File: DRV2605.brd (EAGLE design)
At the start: 49.9 x 25 mm, 60 parts, among them J1 BM06B-SRSS-TB, J2 BM06B-SRSS-TB, J3 BM06B-SRSS-TB, J4 BM06B-SRSS-TB, J5 BM06B-SRSS-TB, U1 DRV2605L, U2 DRV2605L, U3 DRV2605L, U4 DRV2605L, U5 DRV2605L, U6 DRV2605L, U7 DRV2605L, U8 TCA9548APWR, U9 TCA9548APWR

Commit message: NRF done STM in progress
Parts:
- added C17, C18, C46, C47, C55, C56: 12pF, Nordic_nRF:RESC0402_N
- added C19, C20: 22pF, Nordic_nRF:RESC0402_N
- added C21: 0.1uf, rcl:C0402
- added C22: 10uf, rcl:C0402
- added C23, C24: 2.2uf, rcl:C0402
- added C48: 2.2nF, Nordic_nRF:RESC0402_N
- added C49, C52: 100nF, Nordic_nRF:RESC0402_N
- added C50: 47nF, Nordic_nRF:RESC0402_N
- added C51: 1.0nF, Nordic_nRF:RESC0402_N
- added C53: 4.7µF, Nordic_nRF:RESC0603_N
- added C54: 1.0µF, Nordic_nRF:RESC0603_N
- added C57: 2.2pF, Nordic_nRF:RESC0402_N
- added C58: 1.0pF, Nordic_nRF:RESC0402_N
- added C59: 1.5pF, Nordic_nRF:RESC0402_N
- added L11: 3.3nH, Nordic_nRF:RESC0402_N
- added L12: 10µH, Nordic_nRF:RESC0603_N
- added L13: 15nH, Nordic_nRF:RESC0402_N
- added L14: 4.7nH, Nordic_nRF:RESC0402_N
- added L15: 10nH, Nordic_nRF:RESC0402_N
- added R21, R22, R25: 10k, resistor:R0402
- added R23: 1M, resistor:R0402
- added U$9: STM32F405RGT6, SparkFun-IC-Microcontroller:TQFP64
- added U11: NRF51X22_QFQF, Nordic_nRF:QFN40P600X600X90-48_N
- added X1, X5: 32.768kHz, Nordic_nRF:XTAL_3215_N
- added X2: 8MHz, Nordic_nRF:XTAL_3215_N
- added X4: 16MHz, Nordic_nRF:BT-XTAL_2016_N
- moved C13 28.4 mm to (13.2, 13.7), turned to 270 degrees
- moved I2C14 26.0 mm to (14.8, 16.6), turned to 90 degrees
- moved U7 25.7 mm to (15.5, 15.6), turned to 270 degrees
- moved C16 25.6 mm to (37.9, 26.7)
- moved R18 25.1 mm to (38.0, 24.8)
- moved R19 25.1 mm to (38.0, 23.5)
- moved R20 25.1 mm to (38.0, 22.2)
- moved U9 25.1 mm to (43.2, 23.6)
- moved R14 24.2 mm to (16.2, 16.6), turned to 270 degrees
- moved C14 23.6 mm to (17.7, 16.7), turned to 270 degrees
- moved R13 22.4 mm to (17.7, 16.7), turned to 270 degrees
- moved C11 21.3 mm to (19.4, 13.6), turned to 270 degrees
- moved I2C12 18.7 mm to (20.8, 16.6), turned to 90 degrees
- moved U6 18.6 mm to (21.6, 15.5), turned to 270 degrees
- moved R12 17.0 mm to (22.3, 16.5), turned to 270 degrees
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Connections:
- removed net 1SCL: U8.7
- removed net 1SDA: U8.6
- removed net 2SCL: U8.9
- removed net 2SDA: U8.8
- removed net N$22: U8.21
- new net AVDD: C51.1, C54.1, L13.1, U11.35, U11.36
- new net BLE_RX: U$9.42, U11.11
- new net BLE_TX: U$9.43, U11.10
- new net N$2: R25.2, U$9.28
- new net N$3: R22.1, U$9.60
- new net N$33: C46.1, U11.38, X4.3
- new net N$34: L12.1, L13.2
- new net N$35: L12.2, U11.2
- new net N$36: C50.1, U11.29
- new net N$37: C49.1, U11.39
- new net N$38: L14.1, L15.2, U11.31
- new net N$39: C48.1, L15.1, U11.30
- new net N$40: C57.1, L14.2, U11.32
- new net N$41: C57.2, C58.1, L11.1
- new net N$5: C23.1, U$9.31
- new net N$6: C24.1, U$9.47
- new net P0.00: U11.4
- new net P0.01: U11.5
- new net P0.02: U11.6
- new net P0.03: U11.7
- new net P0.04: U11.8
- new net P0.05: U11.9
- new net P0.08: U11.14
- new net P0.09: U11.15
- new net P0.10: U11.16
- new net P0.11: U11.17
- new net P0.12: U11.18
- new net P0.13: U11.19
- new net P0.14: U11.20
- new net P0.17: U11.25
- new net P0.19: U11.27
- new net P0.20: U11.28
- new net P0.21: U11.40
- new net P0.22: U11.41
- new net P0.23: U11.42
- new net P0.24: U11.43
- new net P0.25: U11.44
- new net P0.26/XL1: C19.2, R23.2, U$9.5, X2.1
- new net P0.26/XL2: C17.2, C55.2, U$9.3, U11.45, X1.1, X5.1
- new net P0.27/XL1: C18.2, C56.2, U$9.4, U11.46, X1.2, X5.2
- new net P0.27/XL2: C20.2, R23.1, U$9.6, X2.2
- new net P0.28: U11.47
- new net P0.29: U11.48
- new net P0.30: U11.3
- new net RF: C59.1, L11.2
- new net RST: R21.2, U$9.7
- new net SWDCLK: U11.24
- new net SWDIO: U11.26
- new net SWDIO/NRESET: U11.23
- new net VDDA: C21.1, C22.1, R21.1, U$9.13
- new net VDD_NRF: C52.1, C53.1, U11.1, U11.12
- new net X2: C47.1, U11.37, X4.1
- net +OUT1: now also J1.2; no longer J1.3
- net +OUT2: now also J2.2; no longer J2.3
- net +OUT3: now also J3.2; no longer J3.3
- net +OUT4: now also J4.2; no longer J4.3
- net +OUT5: now also J5.2; no longer J5.3
- net -OUT1: now also J1.3; no longer J1.2
- net -OUT2: now also J2.3; no longer J2.2
- net -OUT3: now also J3.3; no longer J3.2
- net -OUT4: now also J4.3; no longer J4.2
- net -OUT5: now also J5.3; no longer J5.2
- net GND: now also C17.1, C18.1, C19.1, C20.1, C21.2, C22.2, C23.2, C24.2, C46.2, C47.2, C48.2, C49.2, C50.2, C51.2, C52.2, C53.2, C54.2, C55.1, C56.1, C58.2, C59.2, R22.2, R25.1, U$9.12, U11.13, U11.33, U11.34, U11.PAD, U11.PAD@VIA01, U11.PAD@VIA02, U11.PAD@VIA03, U11.PAD@VIA04, U11.PAD@VIA05, U11.PAD@VIA06, U11.PAD@VIA07, U11.PAD@VIA08, U11.PAD@VIA09, U11.PAD@VIA10, U11.PAD@VIA11, U11.PAD@VIA12, U11.PAD@VIA13, U11.PAD@VIA14, U11.PAD@VIA15, U11.PAD@VIA16, U8.21, X4.2, X4.4
- net INPUTSCL: now also U$9.29
- net INPUTSCL1: now also U$9.58
- net INPUTSDA: now also U$9.30
- net INPUTSDA1: now also U$9.59
- net SCL6: now also U8.9
- net SCL7: now also U8.7
- net SDA6: now also U8.8
- net SDA7: now also U8.6
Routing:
- net COMMON_EN: track 0.00 -> 84.9 mm, vias 0 -> 2
- net SCL6: track 4.07 -> 26.9 mm, vias 1 -> 2
- net GND: track 0.00 -> 22.9 mm, vias 1 -> 28
- net IN/TRIG1: track 0.00 -> 22.7 mm, vias 0 -> 1
- net EN1: track 6.16 -> 25.8 mm
- net SDA6: track 3.29 -> 21.2 mm, vias 1 -> 2
- net AVDD: track 0.00 -> 16.7 mm, vias 0 -> 2
- net IN/TRIG2: track 0.00 -> 16.2 mm, vias 0 -> 1
- net +OUT7: track 6.76 -> 22.2 mm, vias 0 -> 2
- net EN2: track 4.84 -> 19.0 mm
- net IMU_SDA2: track 26.6 -> 40.6 mm
- net -OUT7: track 7.06 -> 20.8 mm, vias 0 -> 2
- net IMU_SCL2: track 23.2 -> 36.6 mm
- net SCL7: track 3.87 -> 16.5 mm, vias 1 -> 2
- net VCC: track 109.5 -> 97.0 mm
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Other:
- board size 49.9 x 25 mm -> 49.9 x 35 mm

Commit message: NRF done STM in progress
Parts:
- added C25, C26, C27, C28, C29, C30: 0.1uf, rcl:C0402
- added C31: 10uf, rcl:C0402
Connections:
- removed net VDDA: C21.1, C22.1, R21.1, U$9.13
- net GND: now also C25.2, C26.2, C27.2, C28.2, C29.2, C30.2, C31.2, U$9.18, U$9.63
- net RST: now also C28.1
- net VCC: now also C21.1, C22.1, C25.1, C26.1, C27.1, C29.1, C30.1, C31.1, R21.1, U$9.1, U$9.13, U$9.19, U$9.32, U$9.48, U$9.64

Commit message: NRF done STM in progress
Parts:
- moved C21 103.0 mm to (73.2, 51.1)
- moved C22 103.0 mm to (73.2, 47.6)
- moved C23 103.0 mm to (73.2, 42.7)
- moved C26 103.0 mm to (73.2, 28.0)
- moved C27 103.0 mm to (73.2, 23.1)
- moved C30 103.0 mm to (73.2, 8.40)
- moved R22 103.0 mm to (73.2, 56.0)
- moved R23 103.0 mm to (73.2, 60.9)
- moved R25 103.0 mm to (73.2, 70.7)
- moved C24 103.0 mm to (73.2, 37.8)
- moved C25 103.0 mm to (73.2, 32.9)
- moved C31 96.4 mm to (47.7, 14.3)
- moved C29 87.1 mm to (47.7, 13.2)
- moved C28 80.4 mm to (47.7, 10.1)
- moved R21 50.4 mm to (47.7, 11.6), turned to 180 degrees
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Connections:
- net P0.26/XL1 renamed PH0
- net P0.27/XL2 renamed PH1
- new net PC14: C17.2, U$9.3, X1.1
- new net PC15: C18.2, U$9.4, X1.2
- net P0.26/XL2: no longer C17.2, U$9.3, X1.1
- net P0.27/XL1: no longer C18.2, U$9.4, X1.2
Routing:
- net +OUT7: track 22.2 -> 11.3 mm, vias 2 -> 0
- net -OUT7: track 20.8 -> 11.7 mm, vias 2 -> 0
- net VCC: track 97.0 -> 103.3 mm
- net RST: track 0.00 -> 4.59 mm
- net +OUT6: track 11.9 -> 8.20 mm
- net -OUT6: track 10.7 -> 8.20 mm
- net GND: track 22.9 -> 24.3 mm

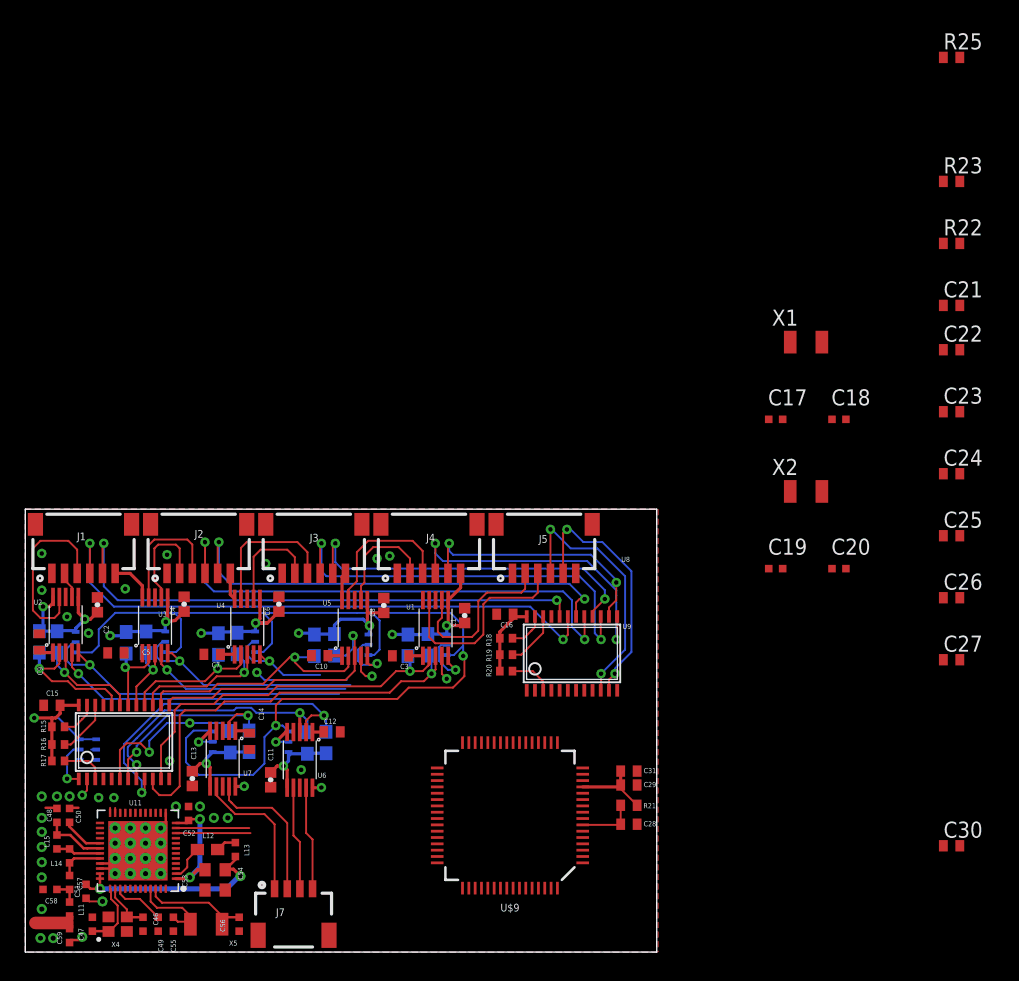
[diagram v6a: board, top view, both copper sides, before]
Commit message: 6DRVs ARM - done; IMU on board
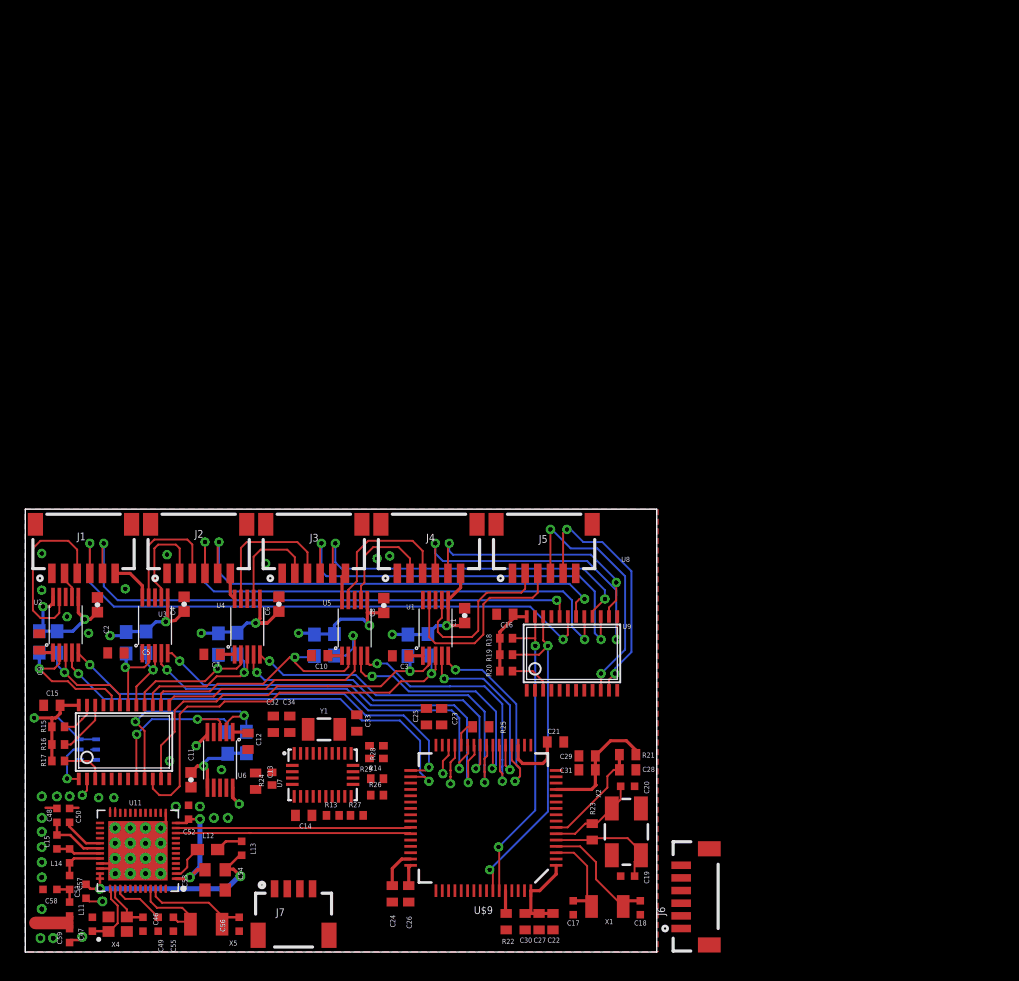
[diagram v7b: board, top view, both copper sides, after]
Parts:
- removed I2C10, I2C12, I2C14, I2C2, I2C4, I2C6, I2C8: JUMPER_3PLACE_NO_XTRA_SMALL, yhtomit_jumpers:XTRA_SMALL_JUMPER_3_NO
- added C32: 0.1uF, rcl:C0402
- added C33, C34: 22pF, rcl:C0402
- added J6: JST_6_PIN_VERTICAL, SparkFun-Connectors:JST-6-SMD-VERT-1.0MM
- added R24: 10k, rcl:R0402
- added R26, R27: 4.7k, rcl:R0402
- added R28, R29: 2.2k, rcl:R0402
- added Y1: 32.768kHz, SparkFun-Clocks:CRYSTAL-SMD-3.2X1.5MM
- C13: value 1.0uF -> 0.1uF; device SparkFun-Capacitors:0402-CAP -> rcl:C0402
- C14: value 1.0uF -> 0.1uF
- R13, R14: value 2.2k -> 10k; device SparkFun-Resistors:0603-RES -> rcl:R0402
- U7: value DRV2605L -> BNO080; device SparkFun-PowerIC:VSSOP-10 -> SparkFun-IC-Special-Function:LGA-28
- X2: device Nordic_nRF:XTAL_3215_N -> SparkFun-Clocks:CRYSTAL-SMD-5X3.2-4PAD
- moved R25 64.7 mm to (36.0, 17.8), turned to 180 degrees
- moved R22 64.1 mm to (38.0, 2.40), turned to 270 degrees
- moved R23 58.7 mm to (44.8, 9.50), turned to 270 degrees
- moved C24 55.3 mm to (29.0, 4.60), turned to 270 degrees
- moved C22 55.1 mm to (41.7, 2.40), turned to 270 degrees
- moved C26 48.9 mm to (30.3, 4.60), turned to 270 degrees
- moved X1 47.3 mm to (46.0, 3.60)
- moved C23 47.0 mm to (32.9, 18.6), turned to 90 degrees
- moved C21 46.6 mm to (41.9, 16.6)
- moved C25 43.9 mm to (31.7, 18.6), turned to 90 degrees
- moved C17 41.8 mm to (43.3, 3.50), turned to 90 degrees
- moved C18 41.7 mm to (48.6, 3.50), turned to 90 degrees
- moved C27 38.6 mm to (40.6, 2.40), turned to 270 degrees
- moved C30 34.2 mm to (39.5, 2.40), turned to 270 degrees
- moved X2 30.4 mm to (47.5, 9.50), turned to 90 degrees
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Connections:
- removed net +OUT7: J7.1, U7.P$7
- removed net -OUT7: J7.2, U7.P$9
- removed net COMMON_EN: I2C10.3, I2C12.3, I2C14.3, I2C2.3, I2C4.3, I2C6.3, I2C8.3
- removed net EN7: I2C14.2, U7.P$5
- removed net IN/TRIG7: U7.P$4
- new net !BOOT: R24.1, U7.4
- new net !CS: U7.18
- new net !INT: U7.14
- new net !RST: R13.1, U7.11
- new net 3.3V: C13.1, C32.1, R13.2, R14.2, R24.2, R26.2, R27.2, R28.2, R29.2, U7.28, U7.3
- new net ADDR/MOSI: R14.1, U7.17
- new net CAP: C14.1, U7.9
- new net N$11: U$9.10
- new net N$12: U$9.11
- new net N$14: C33.1, U7.26, Y1.P$1
- new net N$8: U$9.8
- new net N$9: U$9.9
- new net PS0/WAKE: U7.6
- new net PS1: U7.5
- new net SCL/SCK/RX: R28.1, U7.19
- new net SDA/MISO/TX: R29.1, U7.20
- new net S_SCL: R27.1, U7.15
- new net S_SDA: R26.1, U7.16
- new net TCK: J6.4, U$9.49
- new net TDI: J6.3, U$9.50
- new net TDO: J6.2, U$9.55
- new net TMS: J6.5, U$9.46
- new net TRST: J6.1, U$9.56
- net EN1: now also U$9.33; no longer I2C2.2
- net EN2: now also U$9.26; no longer I2C4.2
- net EN3: now also U$9.24; no longer I2C6.2
- net EN4: now also U$9.22; no longer I2C8.2
- net EN5: now also U$9.20; no longer I2C10.2
- net EN6: no longer I2C12.2
- net GND: now also C32.2, C33.2, C34.2, U7.10, U7.2, U7.25; no longer U7.P$8
- net IN/TRIG1: now also U$9.34
- net IN/TRIG2: now also U$9.27
- net IN/TRIG3: now also U$9.25
- net IN/TRIG4: now also U$9.23
- net IN/TRIG5: now also U$9.21
- net N$7: now also C34.1, U7.27, Y1.P$2; no longer C14.1, U7.P$1
- net PH1: now also X2.3; no longer X2.2
- net RST: now also J6.6
- net SCL7: no longer R13.1, U7.P$2
- net SDA7: no longer R14.1, U7.P$3
- net VCC: no longer C13.1, I2C10.1, I2C12.1, I2C14.1, I2C2.1, I2C4.1, I2C6.1, I2C8.1, R13.2, R14.2, U7.P$10, U7.P$6
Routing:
- net COMMON_EN: track 84.9 -> 0.00 mm, vias 2 -> 0
- net INPUTSCL1: track 4.44 -> 26.9 mm, vias 0 -> 2
- net INPUTSDA1: track 3.13 -> 24.8 mm, vias 0 -> 2
- net EN3: track 8.80 -> 28.3 mm, vias 1 -> 2
- net IN/TRIG3: track 7.35 -> 26.8 mm, vias 1 -> 2
- net IN/TRIG4: track 2.27 -> 19.7 mm, vias 1 -> 2
- net EN4: track 4.97 -> 21.9 mm, vias 1 -> 2
- net SCL7: track 16.5 -> 0.00 mm, vias 2 -> 0
- net IN/TRIG2: track 16.2 -> 32.3 mm, vias 1 -> 2
- net EN2: track 19.0 -> 34.1 mm, vias 1 -> 2
- net IN/TRIG1: track 22.7 -> 36.2 mm, vias 1 -> 2
- net SDA7: track 13.3 -> 0.00 mm, vias 2 -> 0
- net IN/TRIG5: track 1.97 -> 15.2 mm, vias 1 -> 2
- net BLE_TX: track 5.90 -> 18.7 mm
- net BLE_RX: track 5.80 -> 18.6 mm
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
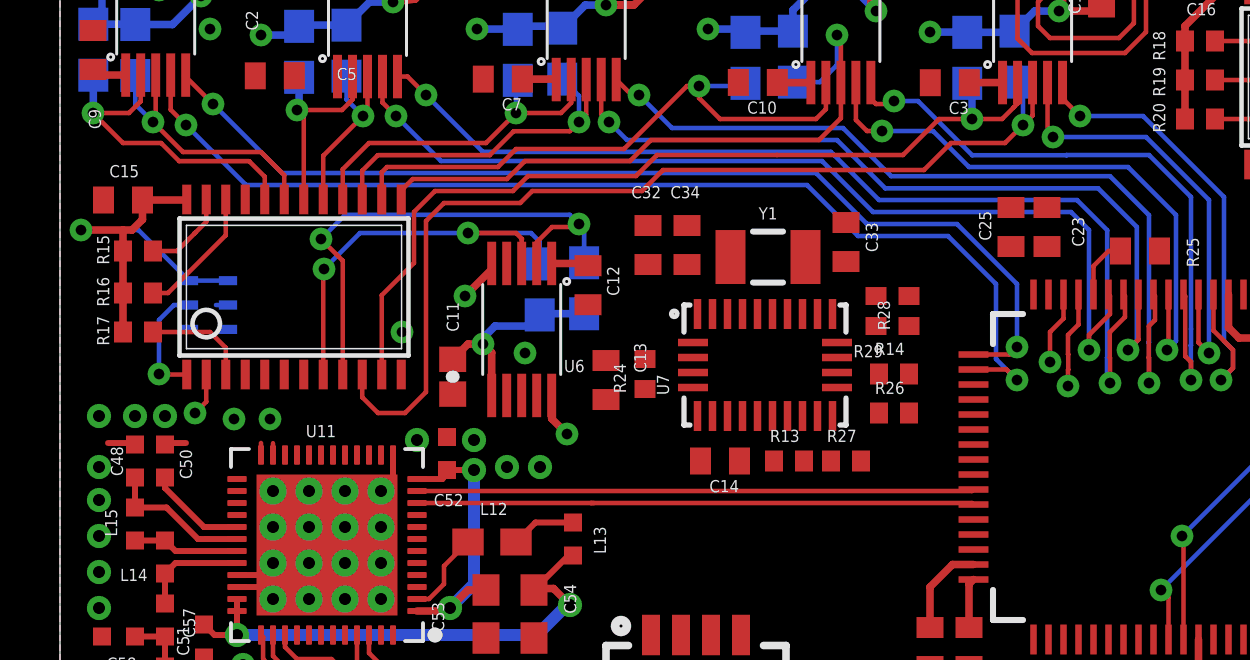
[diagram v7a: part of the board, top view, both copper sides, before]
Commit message: 6DRVs ARM IMU on board - done
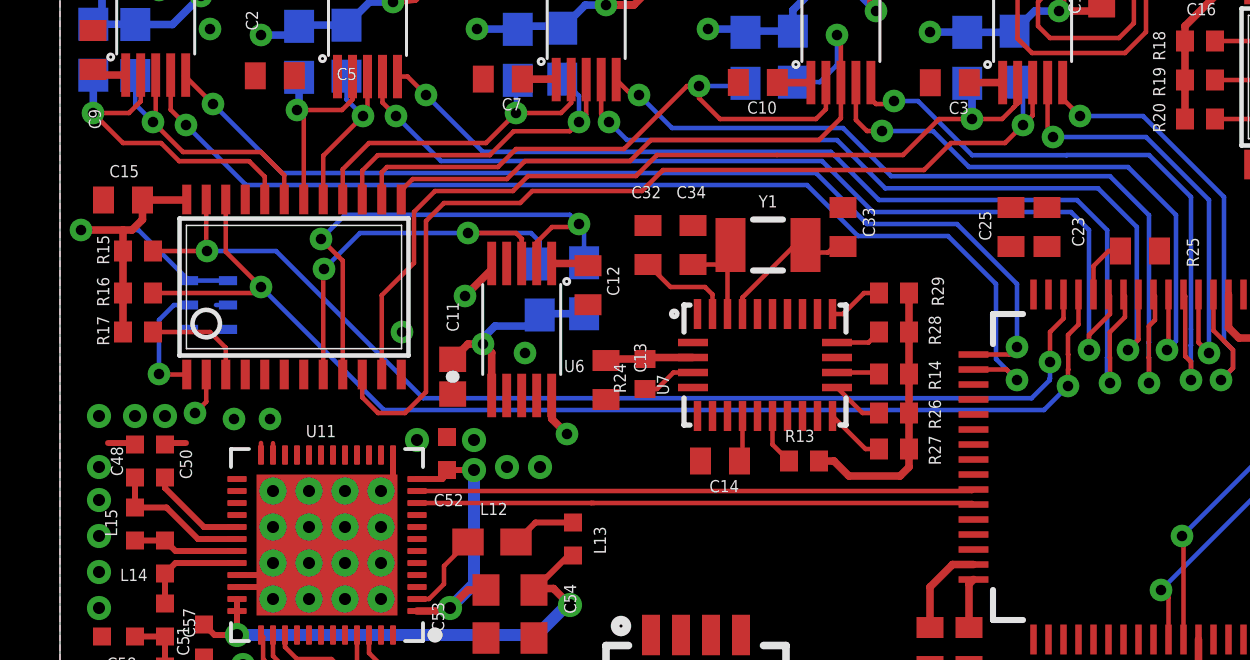
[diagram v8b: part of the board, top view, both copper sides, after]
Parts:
- moved R27 1.65 mm to (27.8, 11.2)
- moved R28 0.86 mm to (27.8, 15.1), turned to 0 degrees
- moved R29 0.85 mm to (27.8, 16.4), turned to 0 degrees
- moved C33 0.51 mm to (26.1, 18.6)
- moved R13 0.50 mm to (24.8, 10.8)
- moved Y1 0.40 mm to (23.6, 18.0)
- moved C34 0.20 mm to (21.1, 18.0)
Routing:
- net INPUTSCL: track 7.62 -> 39.2 mm, vias 1 -> 2
- net INPUTSDA: track 5.37 -> 36.9 mm, vias 1 -> 2
- net 3.3V: track 0.00 -> 15.3 mm
- net N$14: track 0.00 -> 4.96 mm
- net N$7: track 0.00 -> 3.55 mm
- net S_SCL: track 0.00 -> 2.01 mm
- net SDA/MISO/TX: track 0.00 -> 1.84 mm
- net !BOOT: track 0.00 -> 1.83 mm
- net S_SDA: track 0.00 -> 1.75 mm
- net !RST: track 0.00 -> 1.73 mm
- net SCL/SCK/RX: track 0.00 -> 1.54 mm
- net CAP: track 0.00 -> 1.54 mm
- net ADDR/MOSI: track 0.00 -> 1.42 mm
